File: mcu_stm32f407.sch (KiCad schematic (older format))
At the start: 23 parts

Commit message: mmoya/bq76pl536a Adds bq76p536a
TODO: Calculate resistance divider for temp sensors
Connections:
- net labels added: +3V3
- net labels removed: VDD
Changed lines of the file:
@@
 $Descr A4 11693 8268
 encoding utf-8
-Sheet 2 2
+Sheet 2 4
 Title ""
 Date ""
@@
 Text GLabel 2900 2200 0    50   Input ~ 0
 VREF+
-$Comp
-L power:VDD #PWR?
-U 1 1 5FE614BB
-P 4100 1200
-F 0 "#PWR?" H 4100 1050 50  0001 C CNN
-F 1 "VDD" H 4115 1373 50  0000 C CNN
-F 2 "" H 4100 1200 50  0001 C CNN
-F 3 "" H 4100 1200 50  0001 C CNN
-	1    4100 1200
-	1    0    0    -1
-$EndComp
 Wire Wire Line
 	3850 1300 3850 1250
@@
 VBAT
 $Comp
-L power:VDD #PWR?
-U 1 1 5FE7D074
-P 7650 900
-F 0 "#PWR?" H 7650 750 50  0001 C CNN
-F 1 "VDD" H 7665 1073 50  0000 C CNN
-F 2 "" H 7650 900 50  0001 C CNN
-F 3 "" H 7650 900 50  0001 C CNN
-	1    7650 900
-	1    0    0    -1
-$EndComp
-$Comp
 L Device:C C?
 U 1 1 5FE7DFED
@@
 F 3 "~" H 8000 2500 50  0001 C CNN
 	1    8000 2500
-	1    0    0    -1
-$EndComp
-$Comp
-L power:VDD #PWR?
-U 1 1 5FEB7E7F
-P 7100 2200
-F 0 "#PWR?" H 7100 2050 50  0001 C CNN
-F 1 "VDD" H 7115 2373 50  0000 C CNN
-F 2 "" H 7100 2200 50  0001 C CNN
-F 3 "" H 7100 2200 50  0001 C CNN
-	1    7100 2200
 	1    0    0    -1
 $EndComp
@@
 	-1   0    0    -1
 $EndComp
-$Comp
-L power:VDD #PWR?
-U 1 1 5FF036E5
-P 10050 2200
-F 0 "#PWR?" H 10050 2050 50  0001 C CNN
-F 1 "VDD" V 10065 2327 50  0000 L CNN
-F 2 "" H 10050 2200 50  0001 C CNN
-F 3 "" H 10050 2200 50  0001 C CNN
-	1    10050 2200
-	0    -1   -1   0
-$EndComp
 Wire Wire Line
 	10050 2200 10350 2200
@@
 	1    0    0    -1
 $EndComp
-$Comp
-L power:VDD #PWR?
-U 1 1 5FF15C90
-P 3050 1150
-F 0 "#PWR?" H 3050 1000 50  0001 C CNN
-F 1 "VDD" H 3065 1323 50  0000 C CNN
-F 2 "" H 3050 1150 50  0001 C CNN
-F 3 "" H 3050 1150 50  0001 C CNN
-	1    3050 1150
-	1    0    0    -1
-$EndComp
 Wire Wire Line
 	2950 1600 3050 1600
@@
 Text Notes 10550 2500 0    50   ~ 0
 RST
+$Comp
+L power:+3V3 #PWR?
+U 1 1 5FF5411F
+P 4100 1200
+F 0 "#PWR?" H 4100 1050 50  0001 C CNN
+F 1 "+3V3" H 4115 1373 50  0000 C CNN
+F 2 "" H 4100 1200 50  0001 C CNN
+F 3 "" H 4100 1200 50  0001 C CNN
+	1    4100 1200
+	1    0    0    -1
+$EndComp
+$Comp
+L power:+3V3 #PWR?
+U 1 1 5FF546A9
+P 3050 1150
+F 0 "#PWR?" H 3050 1000 50  0001 C CNN
+F 1 "+3V3" H 3065 1323 50  0000 C CNN
+F 2 "" H 3050 1150 50  0001 C CNN
+F 3 "" H 3050 1150 50  0001 C CNN
+	1    3050 1150
+	1    0    0    -1
+$EndComp
+$Comp
+L power:+3V3 #PWR?
+U 1 1 5FF54A00
+P 7650 900
+F 0 "#PWR?" H 7650 750 50  0001 C CNN
+F 1 "+3V3" H 7665 1073 50  0000 C CNN
+F 2 "" H 7650 900 50  0001 C CNN
+F 3 "" H 7650 900 50  0001 C CNN
+	1    7650 900
+	1    0    0    -1
+$EndComp
+$Comp
+L power:+3V3 #PWR?
+U 1 1 5FF54EB4
+P 7100 2200
+F 0 "#PWR?" H 7100 2050 50  0001 C CNN
+F 1 "+3V3" H 7115 2373 50  0000 C CNN
+F 2 "" H 7100 2200 50  0001 C CNN
+F 3 "" H 7100 2200 50  0001 C CNN
+	1    7100 2200
+	1    0    0    -1
+$EndComp
+$Comp
+L power:+3V3 #PWR?
+U 1 1 5FF552E6
+P 10050 2200
+F 0 "#PWR?" H 10050 2050 50  0001 C CNN
+F 1 "+3V3" V 10065 2328 50  0000 L CNN
+F 2 "" H 10050 2200 50  0001 C CNN
+F 3 "" H 10050 2200 50  0001 C CNN
+	1    10050 2200
+	0    -1   -1   0
+$EndComp
 $EndSCHEMATC

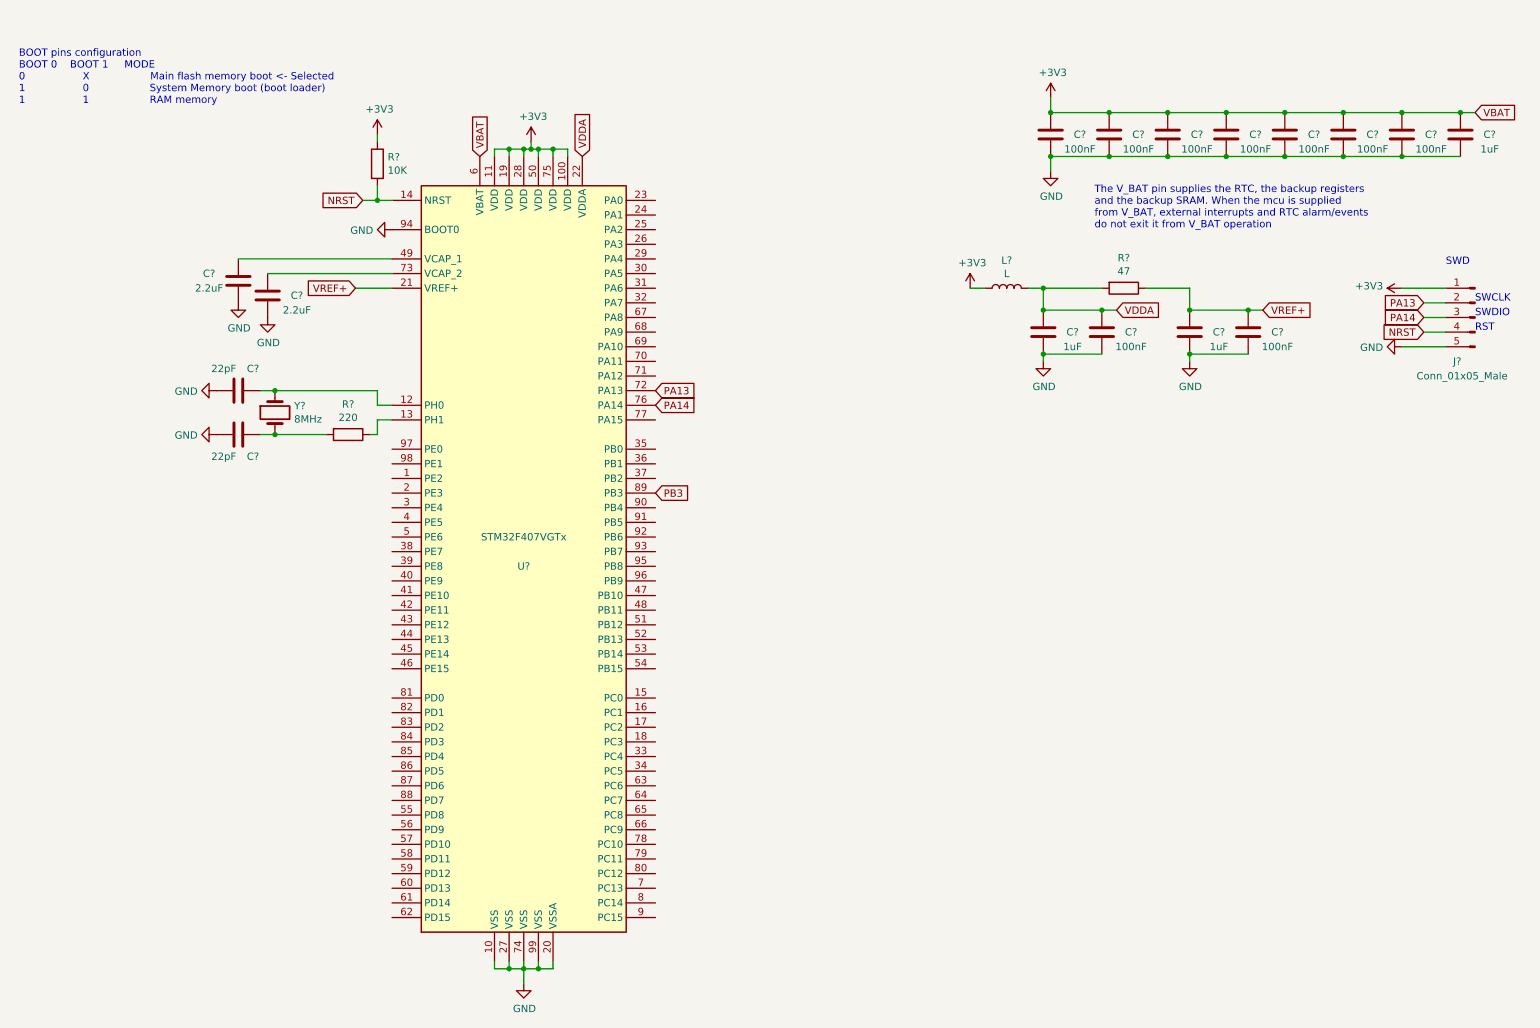
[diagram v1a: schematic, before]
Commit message: Adds missing footprints for conns
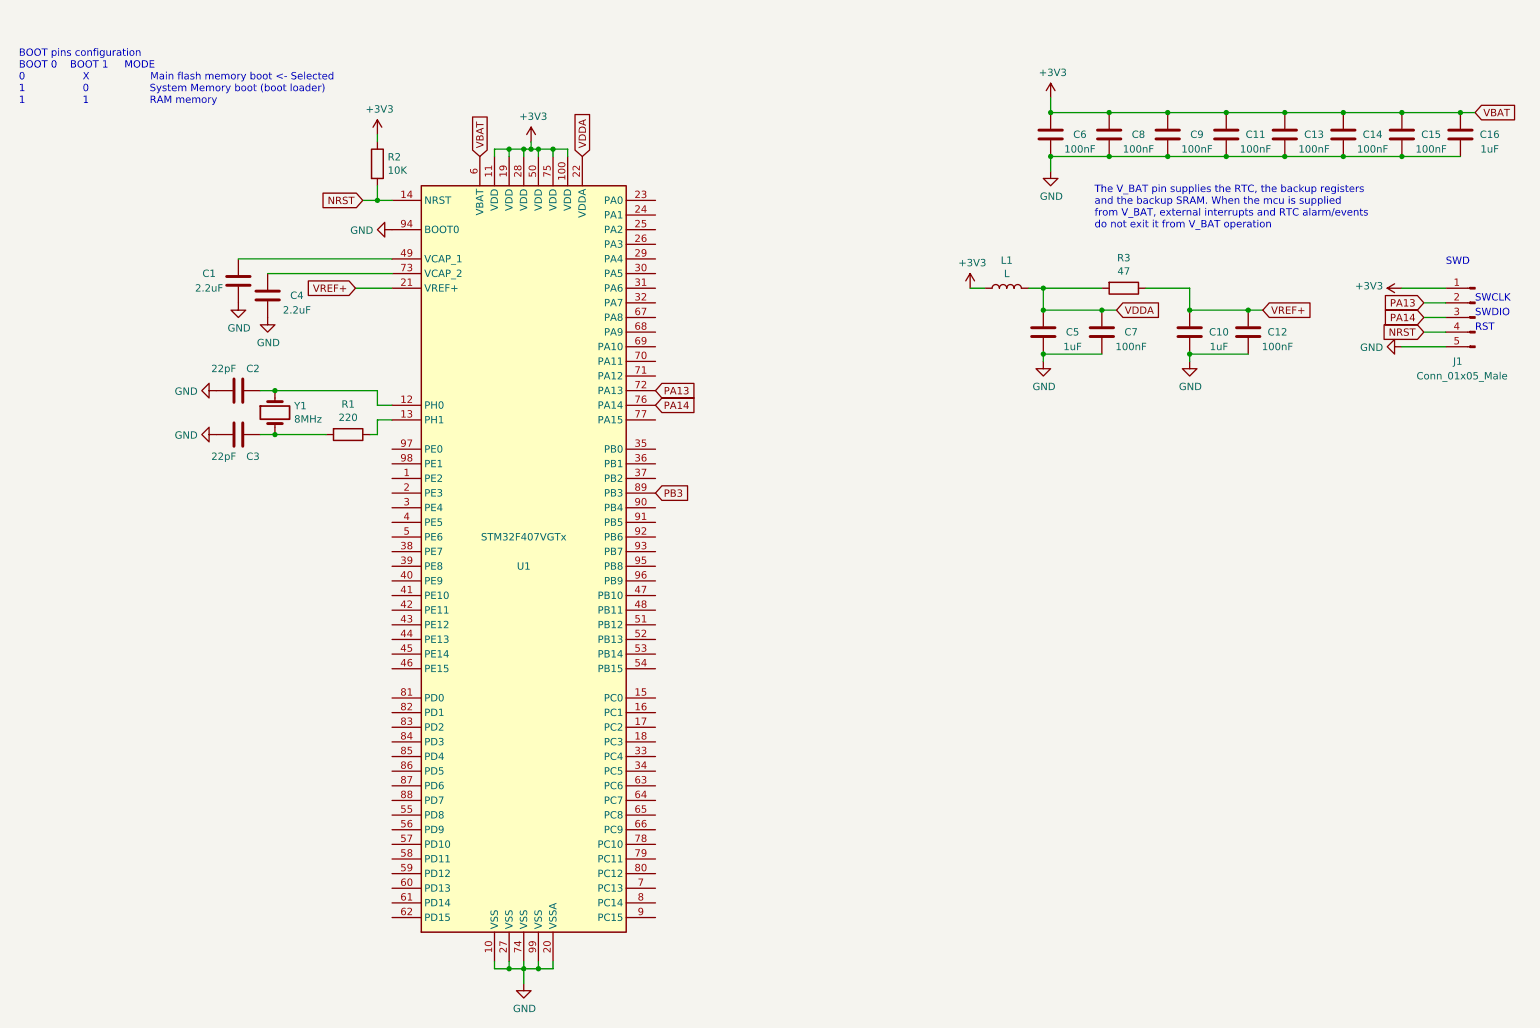
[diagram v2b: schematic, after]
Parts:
- gave numbers to parts that had none: 23

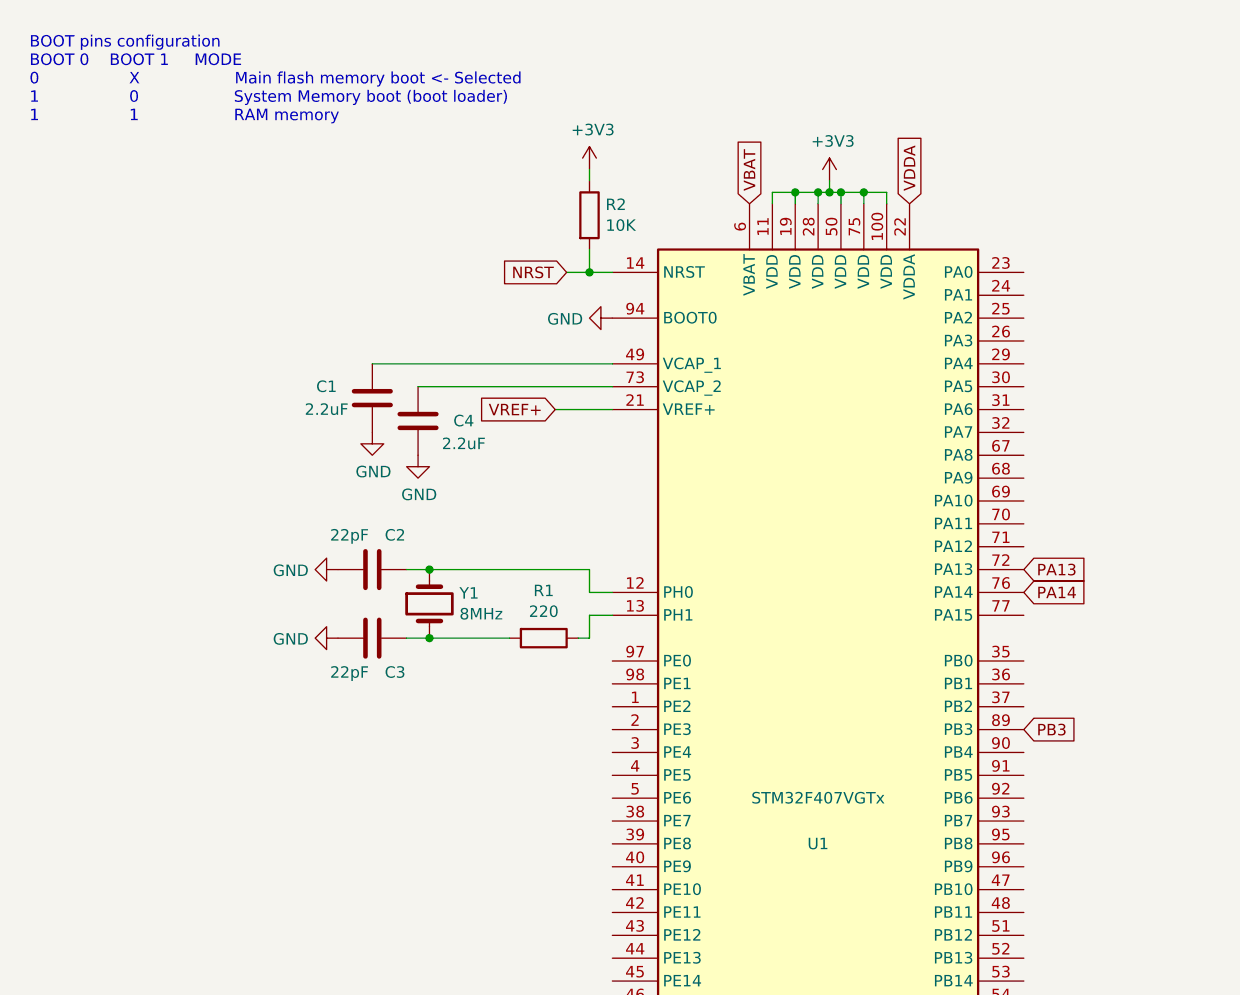
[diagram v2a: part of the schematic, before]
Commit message: mmoya/ina226 Adds ina226 current sensor
- Expects a max current of 20A
- Adds pcb footprint
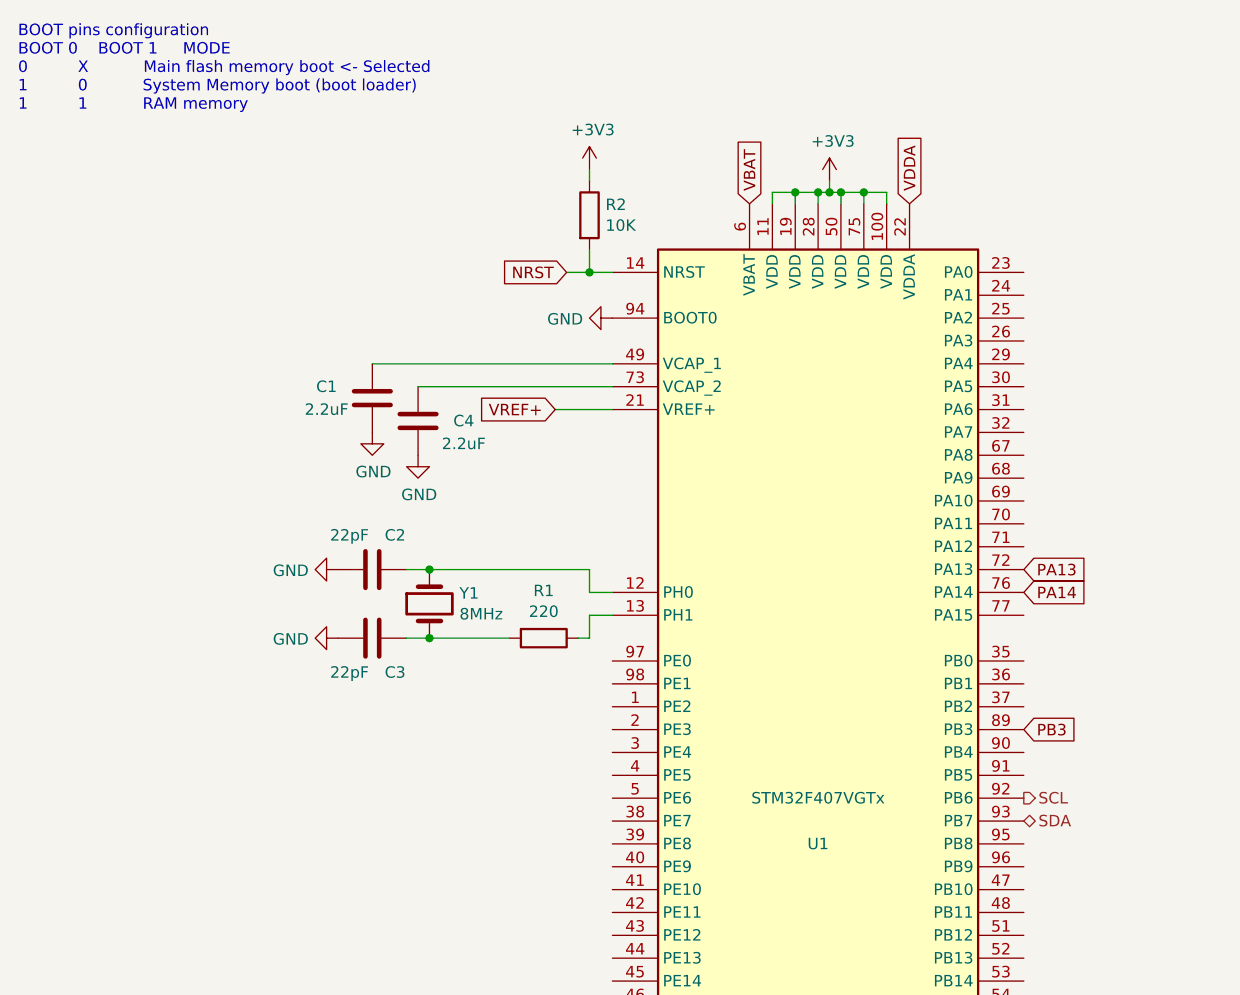
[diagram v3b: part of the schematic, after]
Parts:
- J1: footprint (none) -> Connector_PinHeader_2.54mm:PinHeader_1x05_P2.54mm_Vertical
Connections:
- net SCL: now reaches U1.92 (PB6)
- net SDA: now reaches U1.93 (PB7)
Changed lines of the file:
@@
 $Descr A4 11693 8268
 encoding utf-8
-Sheet 2 4
+Sheet 2 5
 Title ""
 Date ""
@@
 	0    1    1    0
 $EndComp
-Text Notes 600  950  0    50   ~ 0
-BOOT pins configuration\nBOOT 0    BOOT 1     MODE\n0                  X                   Main flash memory boot <- Selected\n1                  0                   System Memory boot (boot loader)\n1                  1                   RAM memory
+Text Notes 550  900  0    50   ~ 0
+BOOT pins configuration\nBOOT 0    BOOT 1     MODE\n0          X           Main flash memory boot <- Selected\n1          0           System Memory boot (boot loader)\n1          1           RAM memory
 Text Notes 10350 2050 0    50   ~ 0
 SWD
@@
 F 0 "J1" H 10700 2100 50  0000 R CNN
 F 1 "Conn_01x05_Male" H 10950 2000 50  0000 R CNN
-F 2 "" H 10550 2400 50  0001 C CNN
+F 2 "Connector_PinHeader_2.54mm:PinHeader_1x05_P2.54mm_Vertical" H 10550 2400 50  0001 C CNN
 F 3 "~" H 10550 2400 50  0001 C CNN
 	1    10550 2400
@@
 	0    -1   -1   0
 $EndComp
+Text HLabel 4950 4000 2    50   BiDi ~ 0
+SDA
+Text HLabel 4950 3900 2    50   Output ~ 0
+SCL
 $EndSCHEMATC
